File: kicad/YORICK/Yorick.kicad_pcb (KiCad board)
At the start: 2 copper layers, 7.4 x 4.9 mm, 72 parts, among them J2 AVR-ISP-6, J3 AudioJack2_SwitchT, J4 USB_B_Micro, J5 AudioJack2_SwitchT, Q1 Q_NJFET_DSG, Q2 Q_NJFET_DSG, SW1 SW_Push, SW2 SW_Push, U1 4069, U2 MCP602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

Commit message: components placed, routing commenced!
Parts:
- removed H1, H10, H11, H12, H2, H3, H4, H5, H6, H7, H8, H9: NotePad, MountingHole:MountingHole_4.3mm_M4_DIN965_Pad
- removed the REF** at (92.2, 87.4)
- removed the REF** at (94.1, 147.3)
- removed the REF** at (94.6, 86.1)
- added J1: Conn_01x12, Yorick:TEETH, F.Cu at (94.0, 147.3)
- added REF**: Lines, Yorick:Lines, F.Cu at (94.0, 73.9)
- moved R12 220.0 mm to (58.8, 107.8)
- moved R11 206.6 mm to (62.1, 107.8)
- moved R10 193.1 mm to (65.4, 107.8)
- moved R9 179.7 mm to (68.7, 107.8)
- moved R27 174.3 mm to (98.7, 69.5), turned to 0 degrees
- moved R17 171.9 mm to (108.8, 73.1), turned to 180 degrees
- moved R8 166.3 mm to (71.9, 107.8)
- moved R28 164.0 mm to (59.8, 67.6)
- moved RV5 163.3 mm to (52.1, 43.8)
- moved C8 158.7 mm to (36.2, 64.9), turned to 90 degrees
- moved C7 158.2 mm to (84.2, 59.9)
- moved R18 157.3 mm to (40.7, 55.4), turned to 90 degrees
- moved TP1 155.4 mm to (75.2, 69.4)
- moved C6 153.4 mm to (40.6, 64.9)
- moved U1 153.3 mm to (93.9, 66.1)
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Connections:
- C5 pad 2: Net-(C5-Pad2) -> Net-(J3-T)
- J3 pad 1: (no net) -> GND
- J3 pad 2: (no net) -> Net-(J3-T)
- J3 pad 3: (no net) -> unconnected-(J3-TN-Pad3)
- J5 pad 1: (no net) -> GND
- J5 pad 2: (no net) -> Net-(J5-T)
- J5 pad 3: (no net) -> unconnected-(J5-TN-Pad3)
- R22 pad 2: Net-(U2B-+) -> Net-(J5-T)
- U2 pad 5: Net-(U2B-+) -> Net-(J5-T)
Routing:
- net Net-(J1-Pin_6): track 0.00 -> 93.0 mm
- net Net-(J1-Pin_5): track 0.00 -> 47.4 mm
- net Net-(J1-Pin_8): track 0.00 -> 45.6 mm
- net Net-(J1-Pin_1): track 0.00 -> 44.5 mm
- net Net-(J1-Pin_10): track 0.00 -> 42.4 mm
- net Net-(J1-Pin_3): track 0.00 -> 41.4 mm
- net Net-(J1-Pin_12): track 0.00 -> 36.7 mm
- net Net-(J1-Pin_7): track 0.00 -> 32.8 mm
- net Net-(J1-Pin_11): track 0.00 -> 25.2 mm
- net Net-(J1-Pin_9): track 0.00 -> 25.0 mm
- net Net-(J1-Pin_4): track 0.00 -> 24.1 mm
- net Net-(J1-Pin_2): track 0.00 -> 23.1 mm
- net Net-(J3-T): track 0.00 -> 21.6 mm
- net Net-(D1-K): track 0.00 -> 15.7 mm
- net Net-(D2-K): track 0.00 -> 15.2 mm
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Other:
- board size 7.4 x 4.9 mm -> 124 x 112 mm

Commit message: Yorick tracing
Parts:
- removed REF**: Lines, Yorick:Lines
- moved D1 32.9 mm to (82.7, 91.3)
- moved R37 32.8 mm to (106.5, 49.8), turned to 90 degrees
- moved D2 30.9 mm to (106.1, 91.3)
- moved TP1 23.8 mm to (51.7, 73.0)
- moved Q1 19.8 mm to (129.0, 60.5)
- moved R22 14.3 mm to (56.2, 69.3), turned to 180 degrees
- moved Q2 12.7 mm to (129.1, 55.1)
- moved TP2 11.2 mm to (40.7, 41.1)
- moved C5 9.86 mm to (133.3, 61.8)
- moved C9 6.05 mm to (96.0, 69.5)
- moved C4 3.21 mm to (82.2, 68.8), turned to -90 degrees
- moved R26 1.69 mm to (102.8, 39.7)
- moved R28 0.87 mm to (58.9, 67.4)
- moved R24 0.69 mm to (96.3, 73.3)
- moved C1 0.52 mm to (114.4, 60.0)
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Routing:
- net VCC: track 0.00 -> 159.3 mm
- net Net-(J1-Pin_12): track 36.7 -> 151.4 mm
- net Net-(U2A--): track 0.00 -> 95.4 mm
- net Net-(R13-Pad2): track 0.00 -> 90.7 mm, vias 0 -> 2
- net /MCU_DOUT1: track 0.00 -> 67.3 mm
- net Net-(R14-Pad2): track 0.00 -> 65.8 mm
- net /MCU_DIN2: track 0.00 -> 65.2 mm
- net /MCU_MOSI: track 0.00 -> 60.3 mm, vias 0 -> 1
- net Net-(Q2-S): track 0.00 -> 57.1 mm
- net Net-(R26-Pad1): track 0.00 -> 57.0 mm
- net Net-(Q1-D): track 0.00 -> 54.3 mm, vias 0 -> 1
- net Net-(Q1-G): track 0.00 -> 51.0 mm
- net Net-(Q1-S): track 0.00 -> 47.7 mm
- net Net-(R27-Pad2): track 0.00 -> 45.8 mm
- net /MCU_DIN1: track 0.00 -> 45.2 mm
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- added copper zone on B.Cu, net GND
- added copper zone on F.Cu, net GND
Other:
- board text added: "BRISTOL COMMUNAL MODULAR"
- board text added: "YORICK PLATFORM v1.0"

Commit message: Yorick pcb silkscreen edit
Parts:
- added REF**: facelines, Yorick:Facelines, F.Cu at (93.6, 79.5)

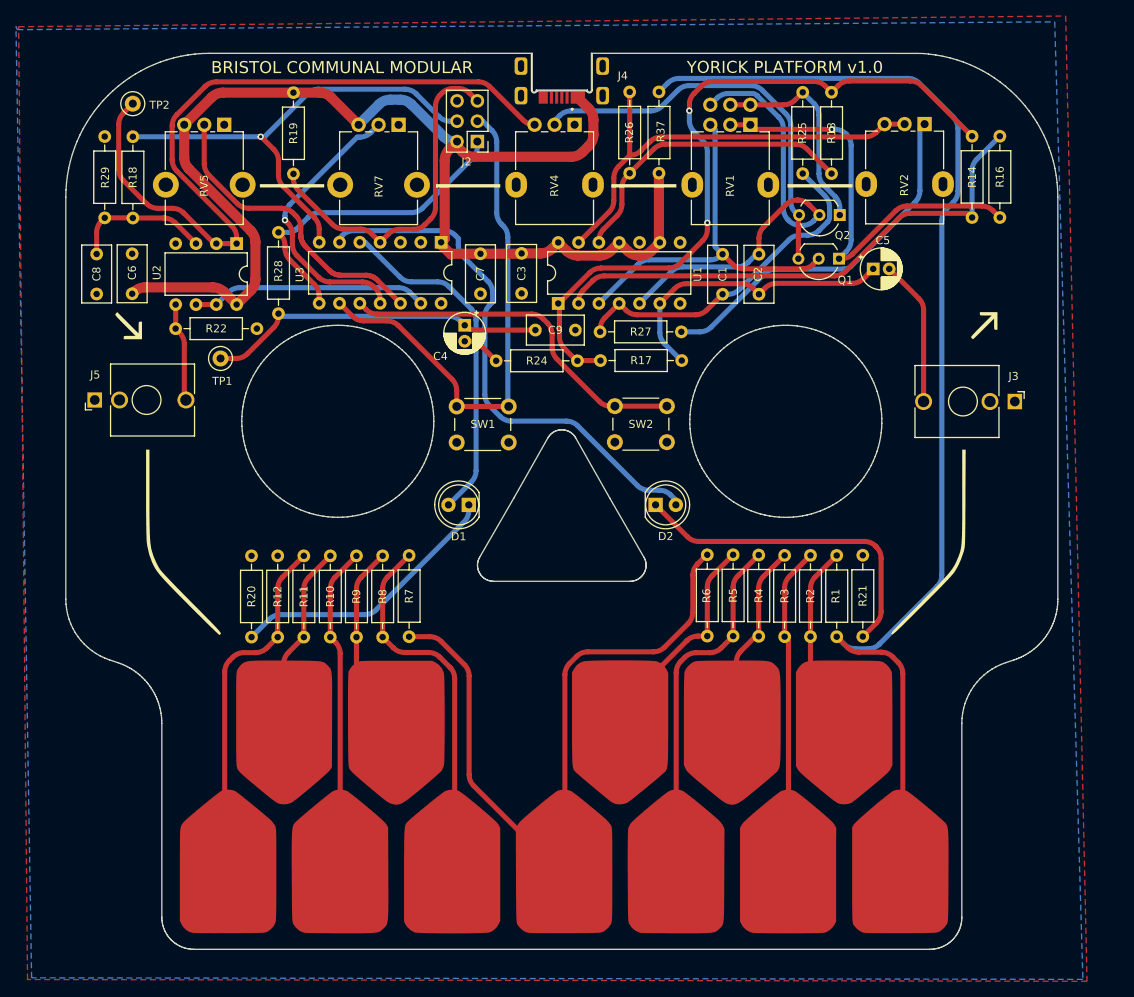
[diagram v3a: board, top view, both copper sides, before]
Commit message: fixing the warnings and simplifying the pcb routing a bit more
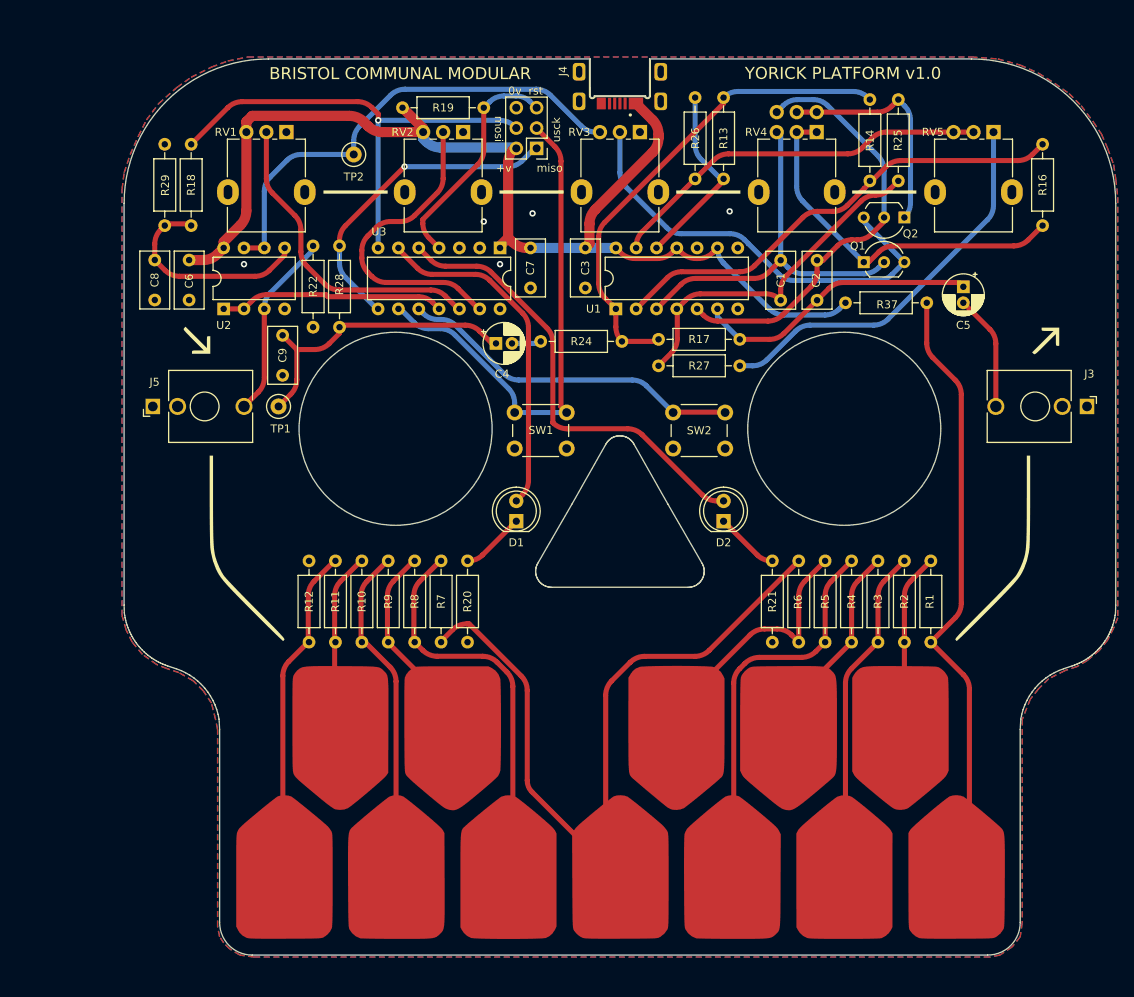
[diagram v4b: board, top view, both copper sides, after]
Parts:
- J4: footprint USBPower:AMPHENOL_10103593-0001LF -> Yorick:AMPHENOL_10103593-0001LF-Power
- RV1: renamed from RV5; footprint Potentiometer_THT:Potentiometer_Alpha_RD901F-40-00D_Single_Vertical_CircularHoles -> Potentiometer_THT:Potentiometer_Alpha_RD901F-40-00D_Single_Vertical
- RV2: renamed from RV7; footprint Potentiometer_THT:Potentiometer_Alpha_RD901F-40-00D_Single_Vertical_CircularHoles -> Potentiometer_THT:Potentiometer_Alpha_RD901F-40-00D_Single_Vertical
- moved C9 37.0 mm to (59.4, 75.1), turned to 90 degrees
- moved R20 28.6 mm to (82.5, 98.3), turned to -90 degrees
- moved R37 28.4 mm to (129.8, 66.0), turned to 0 degrees
- moved TP2 28.3 mm to (68.3, 47.5)
- moved R21 14.7 mm to (120.7, 98.3), turned to -90 degrees
- moved R19 13.8 mm to (74.4, 41.7), turned to 0 degrees
- moved R26 13.6 mm to (111.0, 50.5), turned to 90 degrees
- moved R14 13.6 mm to (132.8, 40.6)
- moved R13 13.5 mm to (114.6, 50.5)
- moved R25 12.0 mm to (136.4, 50.8)
- moved R1 11.8 mm to (140.5, 108.5)
- moved R2 11.8 mm to (137.2, 108.5)
- moved R3 11.7 mm to (133.9, 108.5)
- moved R4 11.6 mm to (130.6, 108.5)
- moved R5 11.5 mm to (127.3, 108.5)
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- renumbered RV4 to RV3, RV1 to RV4, RV2 to RV5
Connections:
- C8 pad 2: Net-(U2A-+) -> Net-(U2B-+)
- R18 pad 1: Net-(U2A-+) -> Net-(U2B-+)
- R29 pad 1: Net-(U2A-+) -> Net-(U2B-+)
- RV3 pad 3: Net-(U2A--) -> Net-(U2B--)
- TP2 pad 1: Net-(U2A--) -> Net-(U2B--)
- U2 pad 1: Net-(U2A--) -> /MCU_ADC_1
- U2 pad 2: Net-(U2A--) -> /MCU_ADC_1
- U2 pad 3: Net-(U2A-+) -> Net-(J5-T)
- U2 pad 5: Net-(J5-T) -> Net-(U2B-+)
- U2 pad 6: /MCU_ADC_1 -> Net-(U2B--)
- U2 pad 7: /MCU_ADC_1 -> Net-(U2B--)
- U3 pad 11: /MCU_ADC_3 -> /MCU_ADC_1
- U3 pad 13: /MCU_ADC_1 -> /MCU_ADC_3
- U3 pad 5: /MCU_DOUT2 -> /MCU_DOUT1
- U3 pad 6: /MCU_DOUT1 -> /MCU_DOUT2
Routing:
- net Net-(U2A--): track 95.4 -> 0.00 mm
- net Net-(J1-Pin_12): track 151.4 -> 74.5 mm
- net Net-(U2B--): track 0.00 -> 60.6 mm
- net Net-(D2-K): track 41.8 -> 8.03 mm
- net Net-(R13-Pad2): track 90.7 -> 61.2 mm, vias 2 -> 0
- net Net-(D1-K): track 34.6 -> 8.03 mm
- net Net-(U2B-+): track 0.00 -> 26.6 mm
- net Net-(U2A-+): track 17.5 -> 0.00 mm
- net Net-(R13-Pad1): track 38.0 -> 23.2 mm
- net /MCU_RESET: track 43.5 -> 28.9 mm
- net VCC: track 159.3 -> 146.3 mm
- net Net-(J5-T): track 12.4 -> 23.4 mm
- net /MCU_DOUT1: track 67.3 -> 57.0 mm
- net Net-(R26-Pad1): track 57.0 -> 48.4 mm
- net Net-(Q1-D): track 54.3 -> 46.1 mm, vias 1 -> 0
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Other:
- outline, holes or cut-outs redrawn
- board text added: "+v"
- board text added: "0v"
- board text added: "miso"
- board text added: "mosi"
- board text added: "rst"
- board text added: "usck"

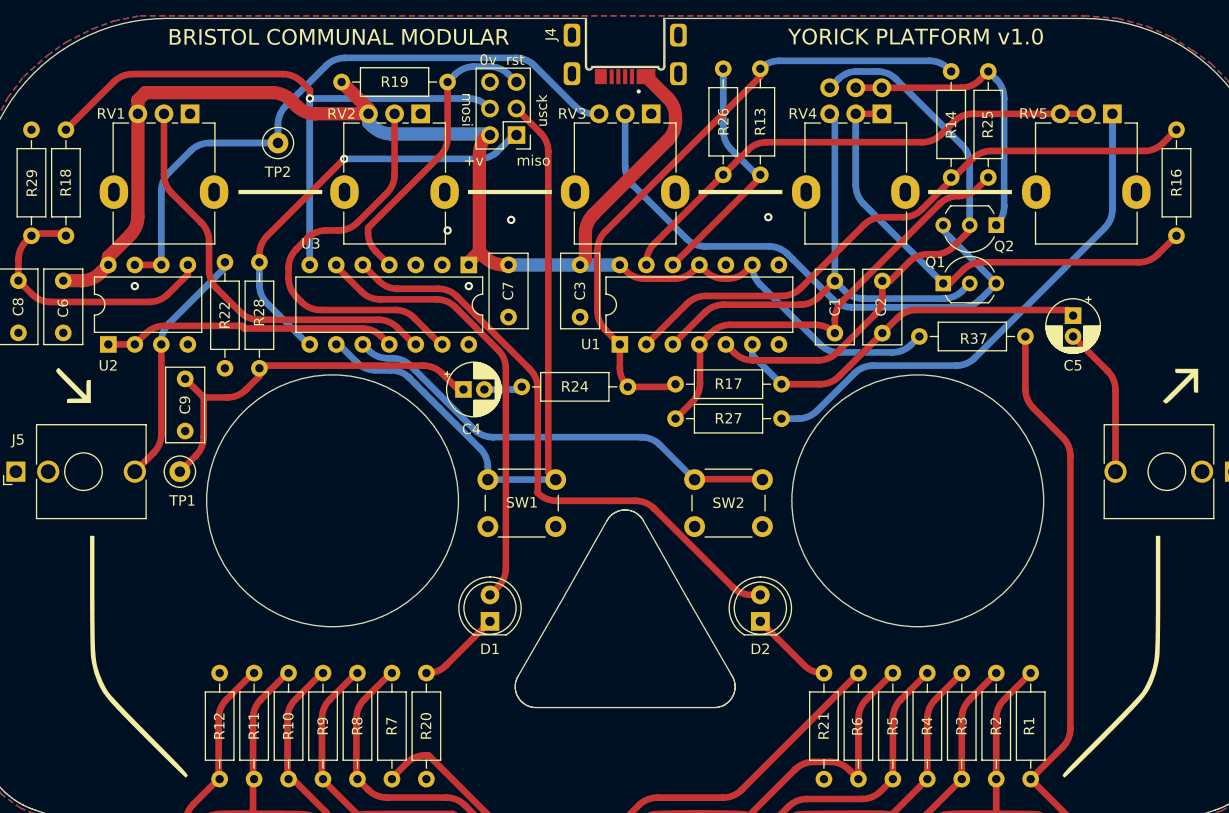
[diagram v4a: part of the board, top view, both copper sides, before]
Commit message: Adding logo, quote, and mounting holes
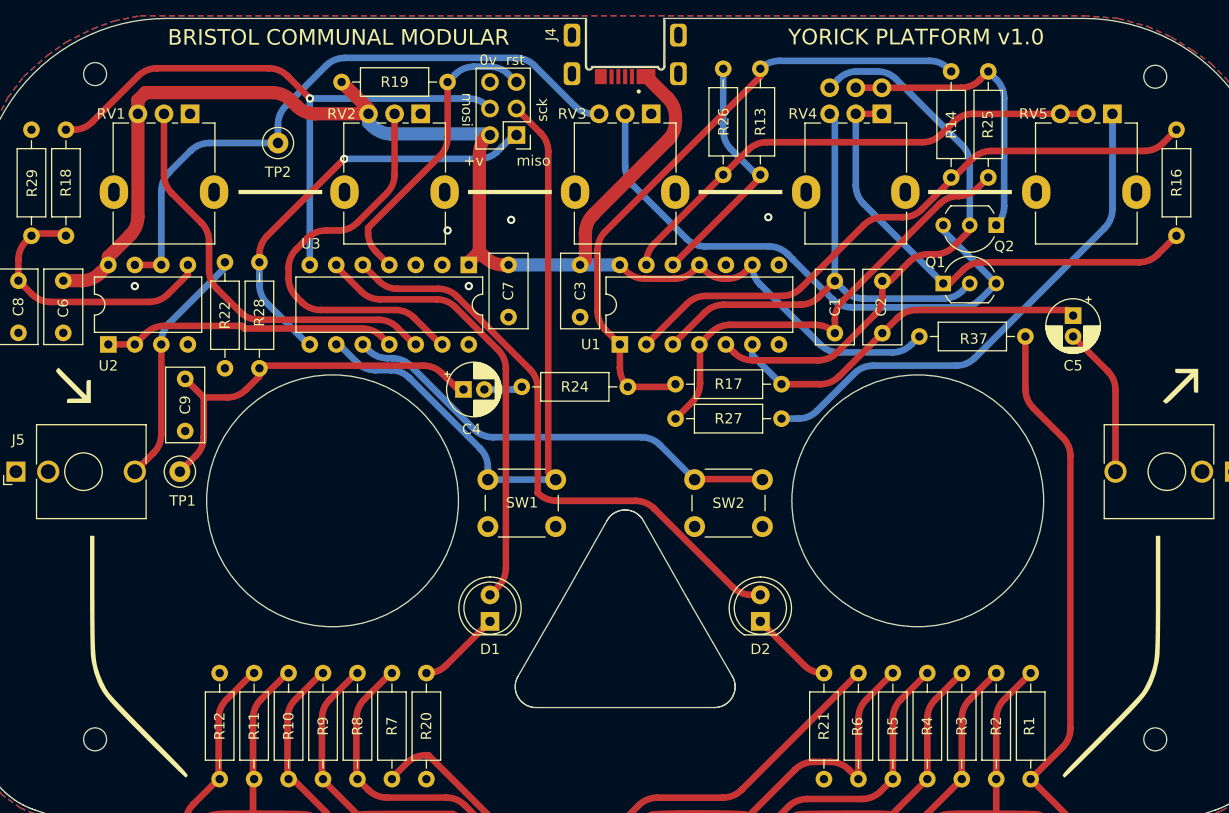
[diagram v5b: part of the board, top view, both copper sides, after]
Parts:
- added H1: MountingHole, MountingHole:MountingHole_2.2mm_M2_DIN965, F.Cu at (152.4, 41.1)
- added H2: MountingHole, MountingHole:MountingHole_2.2mm_M2_DIN965, F.Cu at (50.8, 40.9)
- added H3: MountingHole, MountingHole:MountingHole_2.2mm_M2_DIN965, F.Cu at (50.8, 104.6)
- added H4: MountingHole, MountingHole:MountingHole_2.2mm_M2_DIN965, F.Cu at (152.4, 104.6)
- added Ref**: Val**, BCM_Graphics:BCM_Logo_small_15mmx15mm, B.Cu at (70.4, 126.2)
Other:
- board text added: "Where be your gibes now?"
- board text added: "Your flashes of merriment, that were wont to set the table on a roar?"
- board text added: "Your gambols?"
- board text added: "Your songs?"
- board text added: "sck"
- board text removed: "usck"
